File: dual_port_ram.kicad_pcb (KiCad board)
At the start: 2 copper layers, 27 x 82.5 mm, 3 parts, among them J1 Conn_01x32_MountingPin, J2 Conn_02x32_Counter_Clockwise, J3 Conn_01x32_MountingPin

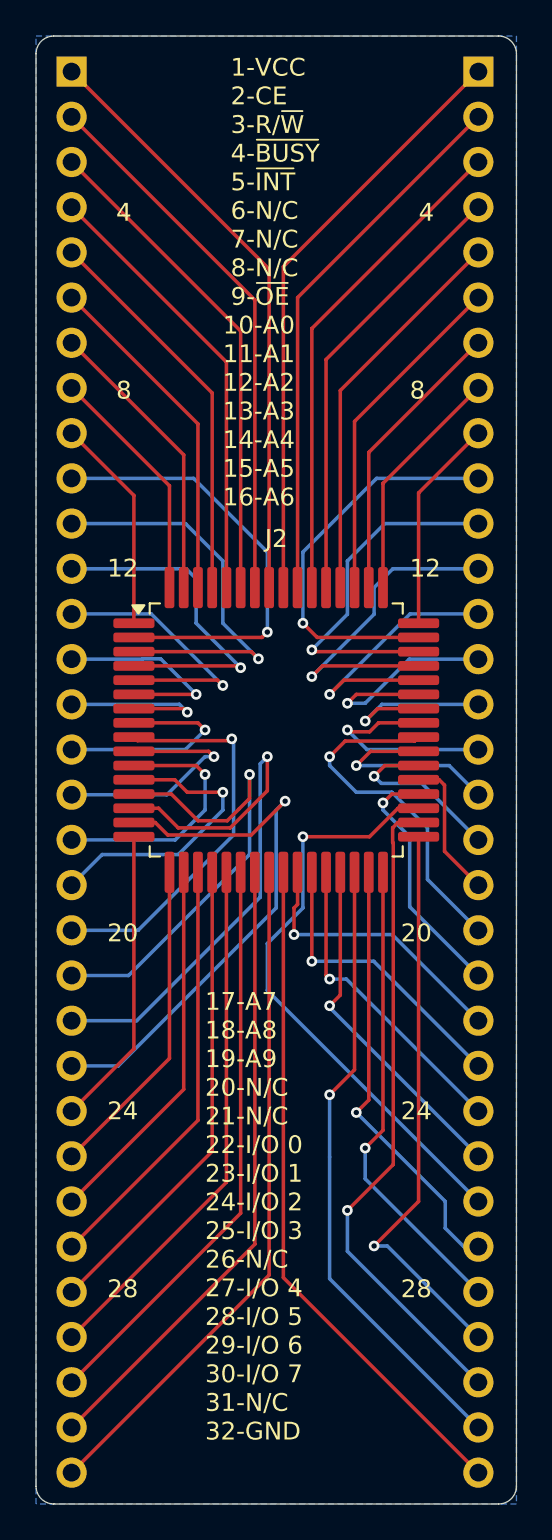
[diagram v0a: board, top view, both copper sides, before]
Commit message: Re-layout parts of board due to schematic changes.
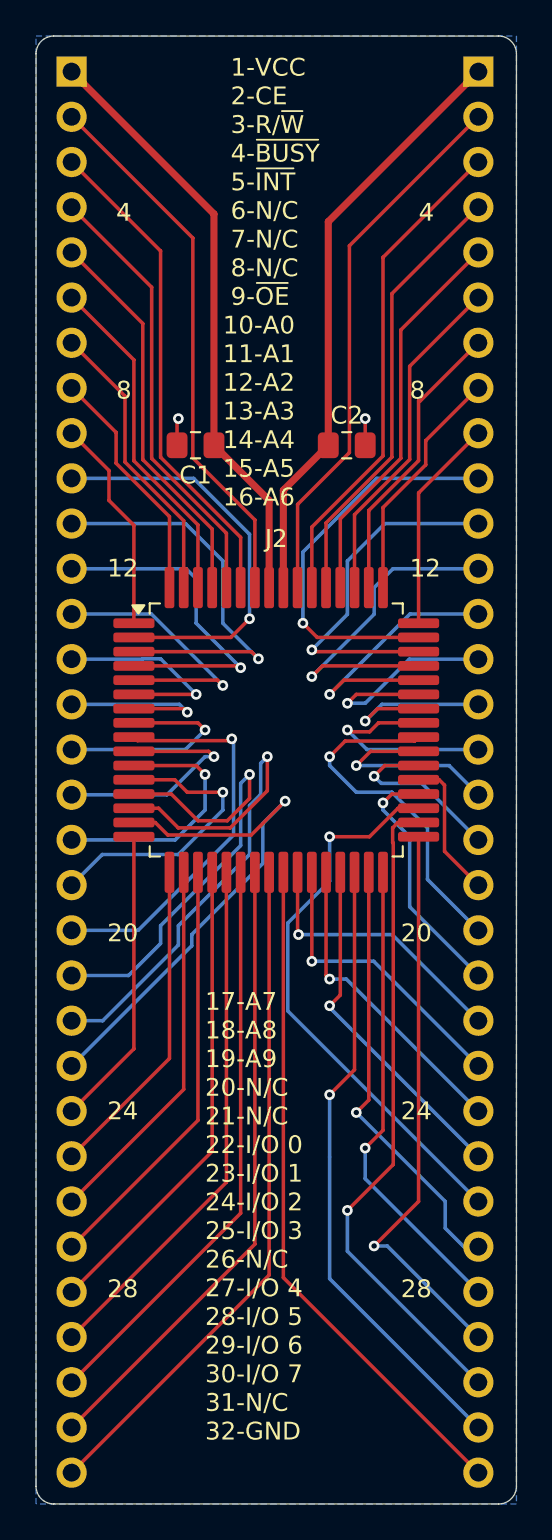
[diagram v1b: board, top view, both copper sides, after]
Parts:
- added C1: 1uF, Capacitor_SMD:C_0805_2012Metric_Pad1.18x1.45mm_HandSolder, F.Cu at (57.0, 71.0)
- added C2: 1uF, Capacitor_SMD:C_0805_2012Metric_Pad1.18x1.45mm_HandSolder, F.Cu at (65.5, 71.0)
- J1, J3: value Conn_01x32_MountingPin -> Conn_01x32
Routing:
- net GND: track 76.6 -> 79.6 mm, vias 0 -> 2
- net /LEFT10: track 24.8 -> 23.0 mm
- net /RIGHT26: track 33.4 -> 31.6 mm
- net /LEFT23: track 31.0 -> 29.4 mm
- net /LEFT22: track 32.3 -> 31.2 mm
